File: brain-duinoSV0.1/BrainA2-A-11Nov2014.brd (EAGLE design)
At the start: 100.1 x 80 mm, 30 parts, among them IC1 OPA2111KP, IC4 OP2177ARMZ

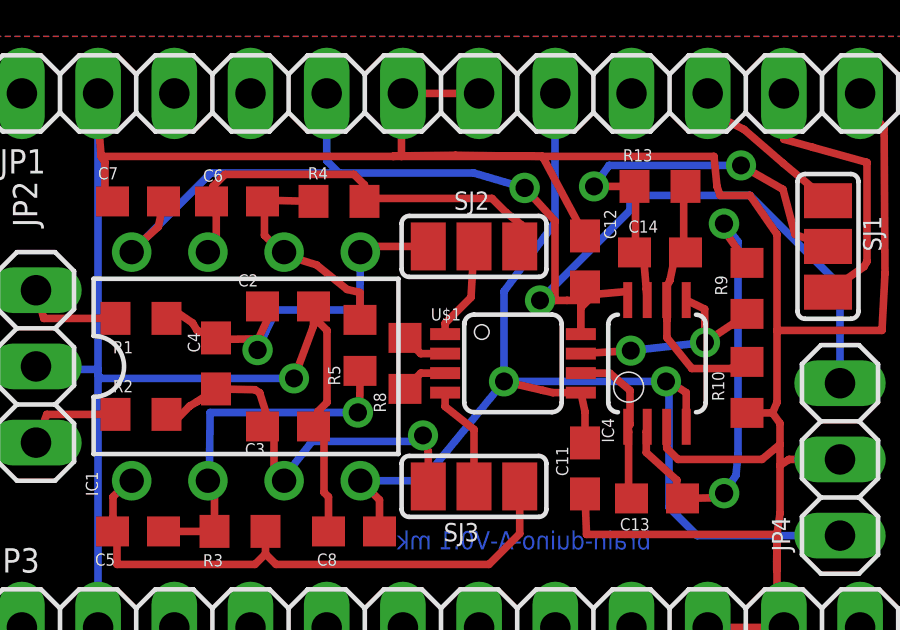
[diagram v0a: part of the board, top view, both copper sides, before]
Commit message: BrainA2-A: Getting rid of some schematic level ERC errors and warnings Renamed U$1 to IC8
Signed-off-by: Christoph Maier <cm.hardware.software.elsewhere@gmail.com>
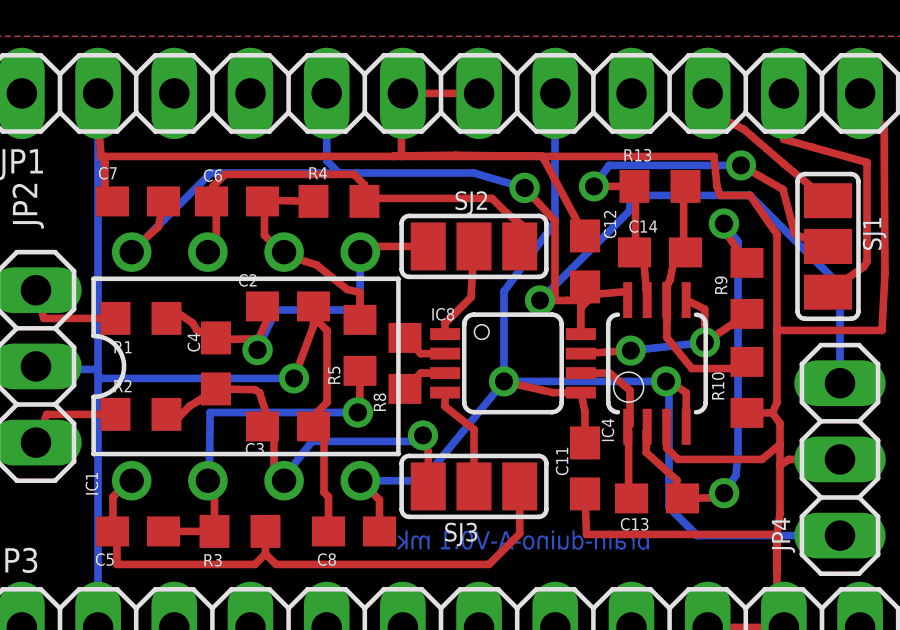
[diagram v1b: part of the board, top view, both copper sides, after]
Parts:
- JP1, JP2, JP3, JP4, SJ1, SJ2, SJ3: value (none) -> .
- renumbered U$1 to IC8
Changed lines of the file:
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@@
 <?xml version="1.0" encoding="utf-8"?>
 <!DOCTYPE eagle SYSTEM "eagle.dtd">
-<eagle version="7.1.0">
+<eagle version="6.5.0">
 <drawing>
 <settings>
@@
 <attribute name="VALUE" x="55.195" y="38.735" size="0.4064" layer="27" rot="R270"/>
 </element>
-<element name="U$1" library="MKH" package="AD8220" value="AD8422ARMZ" x="53.8" y="43" smashed="yes" rot="R270">
+<element name="IC8" library="MKH" package="AD8220" value="AD8422ARMZ" x="53.8" y="43" smashed="yes" rot="R270">
 <attribute name="NAME" x="51.06" y="44.432" size="0.4064" layer="25" ratio="10"/>
 <attribute name="VALUE" x="51.96" y="40.798" size="0.4064" layer="27" ratio="10"/>
@@
 <attribute name="VALUE" x="60.602" y="37.46" size="0.4064" layer="27" ratio="10" rot="R90"/>
 </element>
-<element name="JP1" library="pinhead" package="1X12" value="" x="51.4" y="52" smashed="yes">
+<element name="JP1" library="pinhead" package="1X12" value="." x="51.4" y="52" smashed="yes">
 <attribute name="NAME" x="36.6838" y="49.3288" size="0.8128" layer="25" ratio="10"/>
 <attribute name="VALUE" x="36.16" y="48.825" size="1.27" layer="27"/>
 </element>
-<element name="JP3" library="pinhead" package="1X12" value="" x="51.4" y="34.2" smashed="yes">
+<element name="JP3" library="pinhead" package="1X12" value="." x="51.4" y="34.2" smashed="yes">
 <attribute name="NAME" x="36.4838" y="36.0288" size="0.8128" layer="25" ratio="10"/>
 <attribute name="VALUE" x="36.16" y="31.025" size="1.27" layer="27"/>
 </element>
-<element name="JP2" library="pinhead" package="1X03" value="" x="37.9" y="42.9" smashed="yes" rot="R270">
+<element name="JP2" library="pinhead" package="1X03" value="." x="37.9" y="42.9" smashed="yes" rot="R270">
 <attribute name="NAME" x="37.1288" y="49.0862" size="0.8128" layer="25" ratio="10" rot="R270"/>
 <attribute name="VALUE" x="34.725" y="46.71" size="1.27" layer="27" rot="R270"/>
 </element>
-<element name="SJ1" library="jumper" package="SJ_2" value="" x="64.3" y="46.9" smashed="yes" rot="R270">
+<element name="SJ1" library="jumper" package="SJ_2" value="." x="64.3" y="46.9" smashed="yes" rot="R270">
 <attribute name="NAME" x="65.47" y="47.913" size="0.6096" layer="25" ratio="10" rot="R270"/>
 <attribute name="VALUE" x="64.3" y="47.0001" size="0.02" layer="27" rot="R270"/>
 </element>
-<element name="SJ2" library="jumper" package="SJ_2" value="" x="52.5" y="46.9" smashed="yes" rot="R180">
+<element name="SJ2" library="jumper" package="SJ_2" value="." x="52.5" y="46.9" smashed="yes" rot="R180">
 <attribute name="NAME" x="53.013" y="48.73" size="0.6096" layer="25" ratio="10" rot="R180"/>
 <attribute name="VALUE" x="52.6001" y="46.9" size="0.02" layer="27" rot="R180"/>
 </element>
-<element name="SJ3" library="jumper" package="SJ_2" value="" x="52.5" y="38.9" smashed="yes">
+<element name="SJ3" library="jumper" package="SJ_2" value="." x="52.5" y="38.9" smashed="yes">
 <attribute name="NAME" x="51.487" y="37.07" size="0.6096" layer="25" ratio="10"/>
 <attribute name="VALUE" x="52.3999" y="38.9" size="0.02" layer="27"/>
 </element>
-<element name="JP4" library="pinhead" package="1X03" value="" x="64.7" y="39.8" smashed="yes" rot="R270">
+<element name="JP4" library="pinhead" package="1X03" value="." x="64.7" y="39.8" smashed="yes" rot="R270">
 <attribute name="NAME" x="62.4288" y="37.8862" size="0.6096" layer="25" ratio="10" rot="R270"/>
 <attribute name="VALUE" x="61.525" y="43.61" size="1.27" layer="27" rot="R270"/>
@@
 <wire x1="41.98" y1="47.5545" x2="42.15" y2="48.4" width="0.254" layer="1"/>
 <wire x1="41.1545" y1="46.8135" x2="41.09" y2="46.71" width="0.254" layer="1"/>
-<contactref element="U$1" pad="8"/>
+<contactref element="IC8" pad="8"/>
 <contactref element="IC4" pad="8"/>
 <contactref element="C12" pad="2"/>
@@
 <contactref element="C8" pad="1"/>
 <contactref element="C11" pad="1"/>
-<contactref element="U$1" pad="5"/>
+<contactref element="IC8" pad="5"/>
 <contactref element="IC4" pad="4"/>
 <contactref element="JP1" pad="8"/>
@@
 <signal name="N$19">
 <contactref element="R8" pad="1"/>
-<contactref element="U$1" pad="3"/>
+<contactref element="IC8" pad="3"/>
 <wire x1="51.537" y1="42.676" x2="50.726" y2="42.676" width="0.254" layer="1"/>
 <wire x1="50.726" y1="42.676" x2="50.2" y2="42.15" width="0.254" layer="1"/>
@@
 <signal name="N$23">
 <contactref element="R8" pad="2"/>
-<contactref element="U$1" pad="2"/>
+<contactref element="IC8" pad="2"/>
 <wire x1="51.537" y1="43.326" x2="50.724" y2="43.326" width="0.254" layer="1"/>
 <wire x1="50.724" y1="43.326" x2="50.2" y2="43.85" width="0.254" layer="1"/>
@@
 <contactref element="R9" pad="2"/>
 <contactref element="IC4" pad="5"/>
-<contactref element="U$1" pad="7"/>
+<contactref element="IC8" pad="7"/>
 <wire x1="56.062" y1="43.326" x2="57.726" y2="43.426" width="0.254" layer="1"/>
 <wire x1="57.726" y1="43.426" x2="60.2" y2="43.7" width="0.254" layer="16"/>
@@
 <contactref element="C13" pad="1"/>
 <contactref element="IC4" pad="1"/>
-<contactref element="U$1" pad="6"/>
+<contactref element="IC8" pad="6"/>
 <wire x1="57.654" y1="40.717" x2="57.654" y2="38.6515" width="0.254" layer="1"/>
 <wire x1="57.654" y1="38.6515" x2="57.75" y2="38.5" width="0.254" layer="1"/>
@@
 </signal>
 <signal name="N$14">
-<contactref element="U$1" pad="1"/>
-<contactref element="U$1" pad="1"/>
 <contactref element="SJ2" pad="2"/>
+<contactref element="IC8" pad="1"/>
+<contactref element="IC8" pad="1"/>
 <wire x1="51.537" y1="43.976" x2="51.537" y2="44.337" width="0.254" layer="1"/>
 <wire x1="51.537" y1="44.337" x2="52.4" y2="45.2" width="0.254" layer="1"/>
@@
 </signal>
 <signal name="N$15">
-<contactref element="U$1" pad="4"/>
-<contactref element="U$1" pad="4"/>
 <contactref element="SJ3" pad="2"/>
+<contactref element="IC8" pad="4"/>
+<contactref element="IC8" pad="4"/>
 <wire x1="51.537" y1="42.026" x2="51.537" y2="41.563" width="0.254" layer="1"/>
 <wire x1="51.537" y1="41.563" x2="52.5" y2="40.8" width="0.254" layer="1"/>
